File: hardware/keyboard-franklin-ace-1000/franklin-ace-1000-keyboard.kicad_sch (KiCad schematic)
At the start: 161 parts, among them J1 Conn_02x20_Odd_Even, K1 ESC, K10 A, K11 Z, K12 2 @, K13 W, K14 S, K15 X, K16 3 #, K17 E, K18 D, K19 C, K2 BREAK, K20 4 $, K21 R, K22 F, K23 V, K24 5 &, K25 T, K26 G, K27 B, K28 6 ^, K29 Y, K3 PAUSE, K30 H, K31 N, K32 SPACE_8U, K33 7 &, K34 U, K35 J, K36 M, K37 8 *, K38 I, K39 K, K4 CTRL, K40 , <, K41 9 (, K42 O, K43 L, K44 . >, K45 RIGHT, K46 -, K47 +, K48 *, K49 0 ), K5 TAB, K50 P, K51 ; :, K52 / ?, K53 7, K54 4, K55 1, K56 >, K57 - / _, K58 [ {, K59 ; ", K6 LOCK, K60 SHIFT, K61 8, K62 5, K63 2, K64 0, K65 + / =, K66 ] }, K67 RETURN, K68 LEFT, K69 9, K7 SHIFT, K70 6, K71 3, K72 ., K73 SPACE_1U, K74 TAB2, K8 1 !, K9 Q

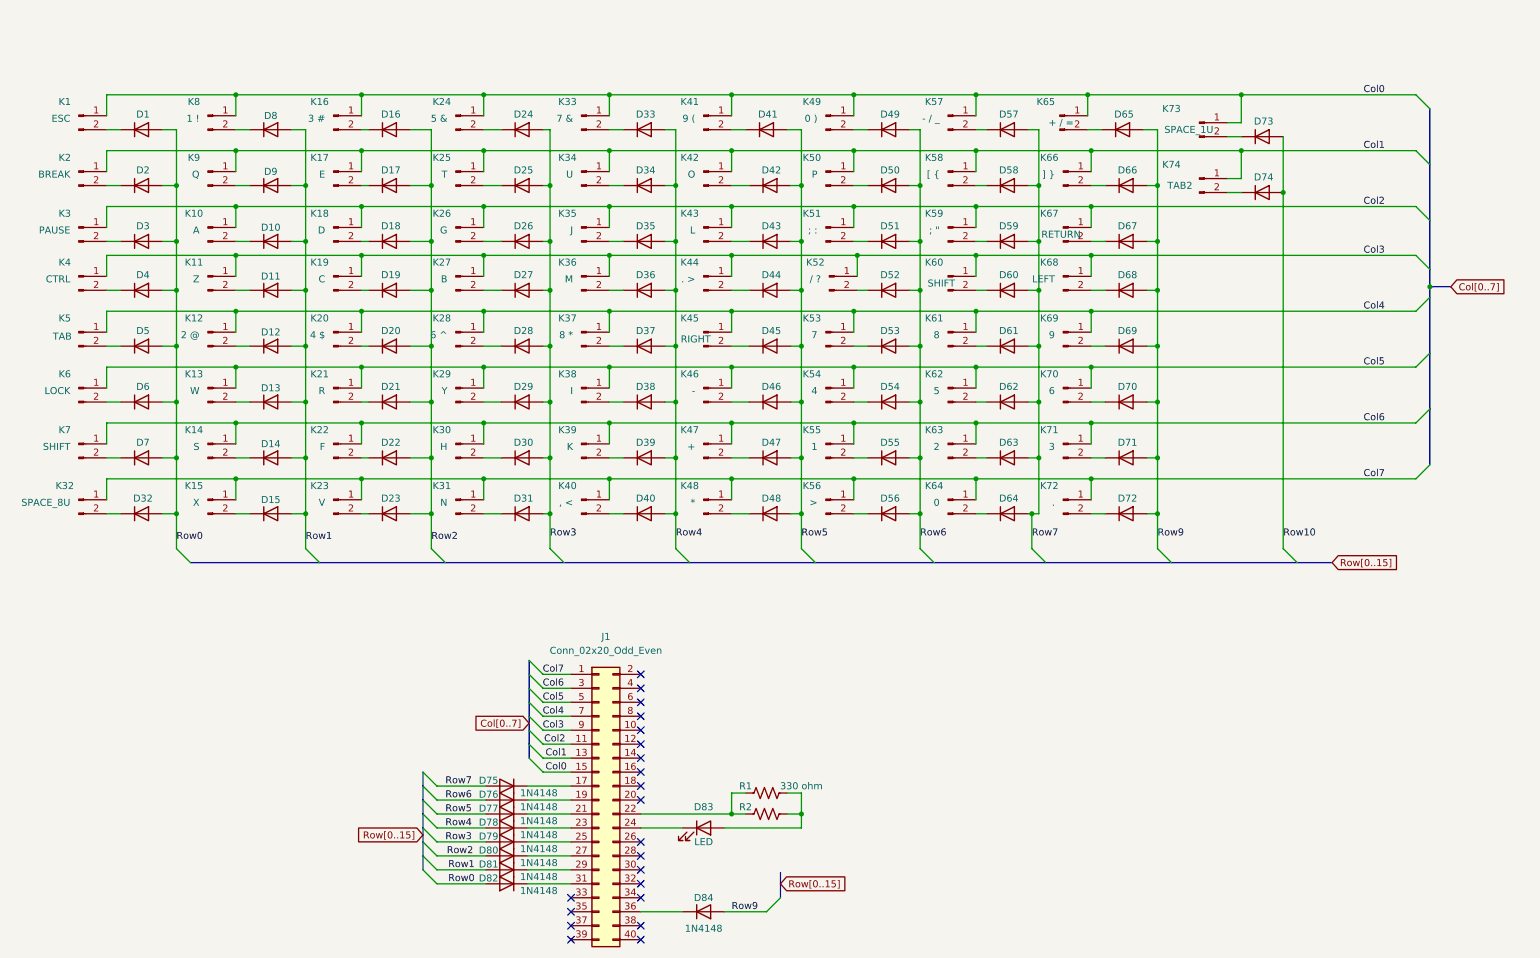
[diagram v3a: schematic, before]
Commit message: True up Franklin 1000 key spacing
- Make sure each 1U is 0.75 inch.
- Record key width for all keys > 1U, and ensure spacing is correct.
- create symbols for the mx keys
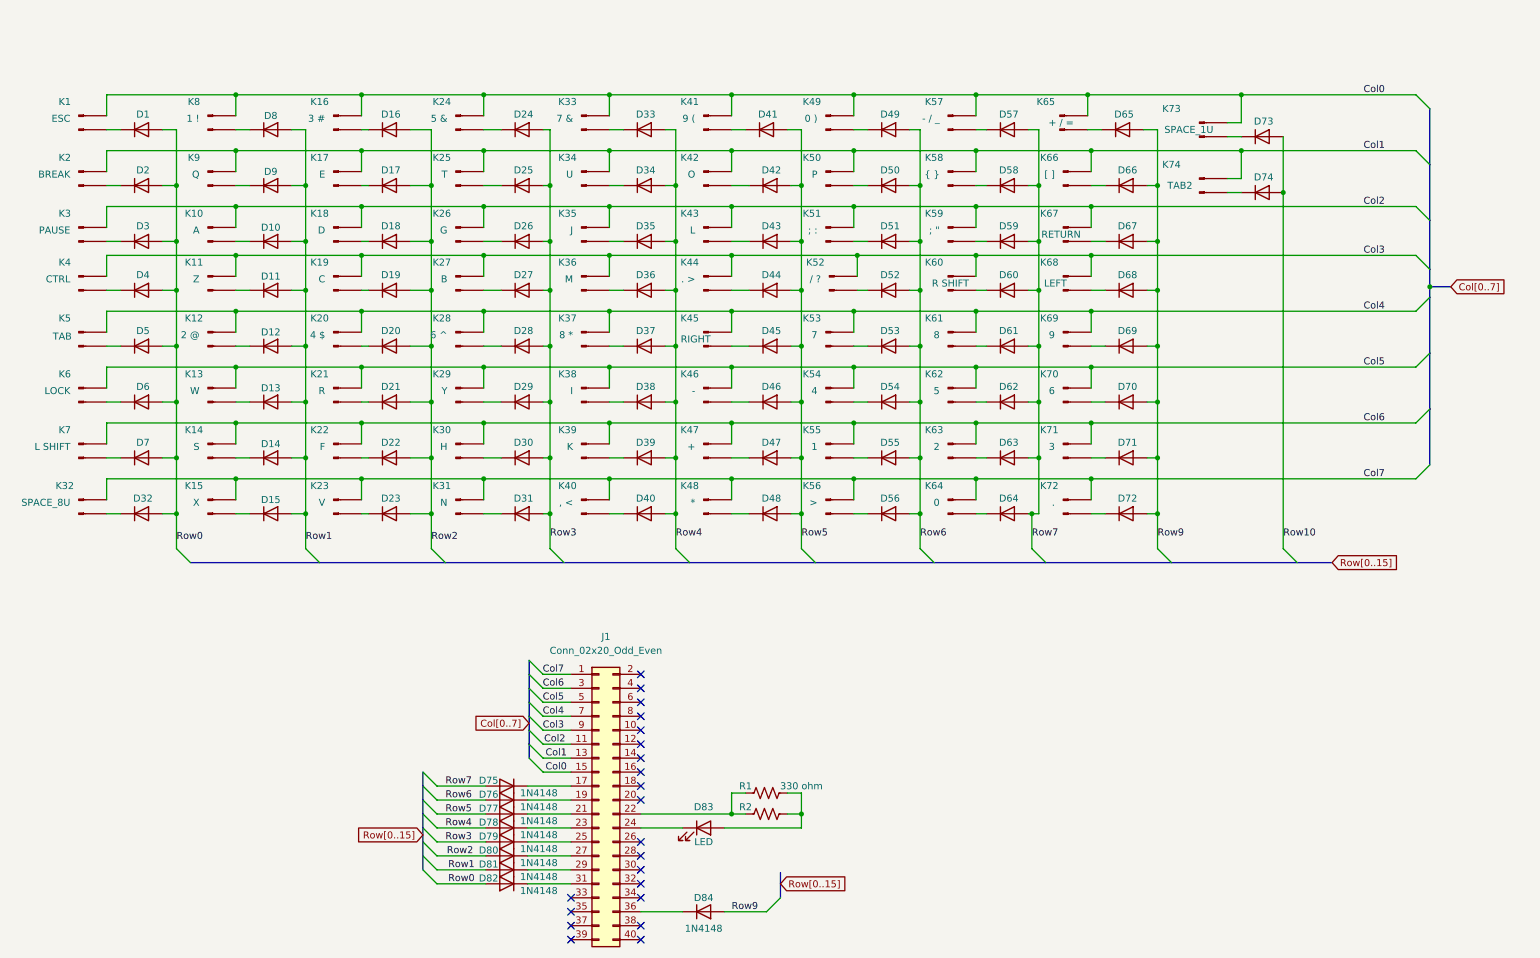
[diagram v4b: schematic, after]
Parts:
- K1, K10, K11, K12, K13, K14, K15, K16, K17, K18, K19, K2, K20, K21, K22, K23, K24, K25, K26, K27, K28, K29, K3, K30, K31, K33, K34, K35, K36, K37, K38, K39, K4, K40, K41, K42, K43, K44, K45, K46, K47, K48, K49, K50, K51, K52, K53, K55, K56, K57, K59, K61, K62, K63, K64, K65, K69, K70, K71, K72, K73, K74, K8, K9: symbol Connector:Conn_01x02_Pin -> unikbd:SW Cherry MX/Futaba 1U Style B; Allow Substitution (none) -> Yes; Class (none) -> If applicable; Component Type (none) -> Switch; Component Value (none) -> Key; Fitted (none) -> Yes; Manufacturer (none) -> Cherry; Manufacturer Link (none) -> https://www.cherrymx.de/en/cherry-mx/mx-original/mx-black.h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; Manufacturer PN (none) -> MX1A-11NN; Material (none) -> If applicable; Number of Pins (none) -> 2; Power Rating (none) -> 10 mA; RoHS (none) -> Yes; RoHS Document Link (none) -> https://www.mouser.com/catalog/additional/Cherry_Electrical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; Standards Version (none) -> 1.1; Temp (Operating) (none) -> -40C/+170C; Temp (Soldering) (none) -> If applicable; Temp Coeff. (none) -> If applicable; Tolerance (none) -> If applicable; Tracking (none) -> No
- K32: symbol Connector:Conn_01x02_Pin -> unikbd:SW Cherry MX/Futaba 8U Spacebar Style B; Allow Substitution (none) -> Yes; Class (none) -> If applicable; Component Type (none) -> Switch; Component Value (none) -> Key; Fitted (none) -> Yes; Manufacturer (none) -> Cherry; Manufacturer Link (none) -> https://www.cherrymx.de/en/cherry-mx/mx-original/mx-black.h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; Manufacturer PN (none) -> MX1A-11NN; Material (none) -> If applicable; Number of Pins (none) -> 2; Power Rating (none) -> 10 mA; RoHS (none) -> Yes; RoHS Document Link (none) -> https://www.mouser.com/catalog/additional/Cherry_Electrical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; Standards Version (none) -> 1.1; Temp (Operating) (none) -> -40C/+170C; Temp (Soldering) (none) -> If applicable; Temp Coeff. (none) -> If applicable; Tolerance (none) -> If applicable; Tracking (none) -> No
- K5, K67: symbol Connector:Conn_01x02_Pin -> unikbd:SW Cherry MX/Futaba 1U Style B; Allow Substitution (none) -> Yes; BOM Comment (none) -> 1.5U; Class (none) -> If applicable; Component Type (none) -> Switch; Component Value (none) -> Key; Fitted (none) -> Yes; Manufacturer (none) -> Cherry; Manufacturer Link (none) -> https://www.cherrymx.de/en/cherry-mx/mx-original/mx-black.h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; Manufacturer PN (none) -> MX1A-11NN; Material (none) -> If applicable; Number of Pins (none) -> 2; Power Rating (none) -> 10 mA; RoHS (none) -> Yes; RoHS Document Link (none) -> https://www.mouser.com/catalog/additional/Cherry_Electrical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; Standards Version (none) -> 1.1; Temp (Operating) (none) -> -40C/+170C; Temp (Soldering) (none) -> If applicable; Temp Coeff. (none) -> If applicable; Tolerance (none) -> If applicable; Tracking (none) -> No
- K54: symbol Connector:Conn_01x02_Pin -> unikbd:SW Cherry MX/Futaba 1U Style B; Allow Substitution (none) -> Yes; BOM Comment (none) -> 2.25 U spacing; Class (none) -> If applicable; Component Type (none) -> Switch; Component Value (none) -> Key; Fitted (none) -> Yes; Manufacturer (none) -> Cherry; Manufacturer Link (none) -> https://www.cherrymx.de/en/cherry-mx/mx-original/mx-black.h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; Manufacturer PN (none) -> MX1A-11NN; Material (none) -> If applicable; Number of Pins (none) -> 2; Power Rating (none) -> 10 mA; RoHS (none) -> Yes; RoHS Document Link (none) -> https://www.mouser.com/catalog/additional/Cherry_Electrical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; Standards Version (none) -> 1.1; Temp (Operating) (none) -> -40C/+170C; Temp (Soldering) (none) -> If applicable; Temp Coeff. (none) -> If applicable; Tolerance (none) -> If applicable; Tracking (none) -> No
- K58: value [ { -> { }; symbol Connector:Conn_01x02_Pin -> unikbd:SW Cherry MX/Futaba 1U Style B; Allow Substitution (none) -> Yes; Class (none) -> If applicable; Component Type (none) -> Switch; Component Value (none) -> Key; Fitted (none) -> Yes; Manufacturer (none) -> Cherry; Manufacturer Link (none) -> https://www.cherrymx.de/en/cherry-mx/mx-original/mx-black.h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; Manufacturer PN (none) -> MX1A-11NN; Material (none) -> If applicable; Number of Pins (none) -> 2; Power Rating (none) -> 10 mA; RoHS (none) -> Yes; RoHS Document Link (none) -> https://www.mouser.com/catalog/additional/Cherry_Electrical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; Standards Version (none) -> 1.1; Temp (Operating) (none) -> -40C/+170C; Temp (Soldering) (none) -> If applicable; Temp Coeff. (none) -> If applicable; Tolerance (none) -> If applicable; Tracking (none) -> No
- K6: symbol Connector:Conn_01x02_Pin -> unikbd:SW Cherry MX/Futaba 1U Style B; Allow Substitution (none) -> Yes; BOM Comment (none) -> 1.75U; Class (none) -> If applicable; Component Type (none) -> Switch; Component Value (none) -> Key; Fitted (none) -> Yes; Manufacturer (none) -> Cherry; Manufacturer Link (none) -> https://www.cherrymx.de/en/cherry-mx/mx-original/mx-black.h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; Manufacturer PN (none) -> MX1A-11NN; Material (none) -> If applicable; Number of Pins (none) -> 2; Power Rating (none) -> 10 mA; RoHS (none) -> Yes; RoHS Document Link (none) -> https://www.mouser.com/catalog/additional/Cherry_Electrical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; Standards Version (none) -> 1.1; Temp (Operating) (none) -> -40C/+170C; Temp (Soldering) (none) -> If applicable; Temp Coeff. (none) -> If applicable; Tolerance (none) -> If applicable; Tracking (none) -> No
- K60: value SHIFT -> R SHIFT; symbol Connector:Conn_01x02_Pin -> unikbd:SW Cherry MX/Futaba 1U Style B; Allow Substitution (none) -> Yes; BOM Comment (none) -> 2U; Class (none) -> If applicable; Component Type (none) -> Switch; Component Value (none) -> Key; Fitted (none) -> Yes; Manufacturer (none) -> Cherry; Manufacturer Link (none) -> https://www.cherrymx.de/en/cherry-mx/mx-original/mx-black.h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; Manufacturer PN (none) -> MX1A-11NN; Material (none) -> If applicable; Number of Pins (none) -> 2; Power Rating (none) -> 10 mA; RoHS (none) -> Yes; RoHS Document Link (none) -> https://www.mouser.com/catalog/additional/Cherry_Electrical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; Standards Version (none) -> 1.1; Temp (Operating) (none) -> -40C/+170C; Temp (Soldering) (none) -> If applicable; Temp Coeff. (none) -> If applicable; Tolerance (none) -> If applicable; Tracking (none) -> No
- K66: value ] } -> [ ]; symbol Connector:Conn_01x02_Pin -> unikbd:SW Cherry MX/Futaba 1U Style B; Allow Substitution (none) -> Yes; BOM Comment (none) -> 1.75U; Class (none) -> If applicable; Component Type (none) -> Switch; Component Value (none) -> Key; Fitted (none) -> Yes; Manufacturer (none) -> Cherry; Manufacturer Link (none) -> https://www.cherrymx.de/en/cherry-mx/mx-original/mx-black.h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; Manufacturer PN (none) -> MX1A-11NN; Material (none) -> If applicable; Number of Pins (none) -> 2; Power Rating (none) -> 10 mA; RoHS (none) -> Yes; RoHS Document Link (none) -> https://www.mouser.com/catalog/additional/Cherry_Electrical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; Standards Version (none) -> 1.1; Temp (Operating) (none) -> -40C/+170C; Temp (Soldering) (none) -> If applicable; Temp Coeff. (none) -> If applicable; Tolerance (none) -> If applicable; Tracking (none) -> No
- K68: symbol Connector:Conn_01x02_Pin -> unikbd:SW Cherry MX/Futaba 1U Style B; Allow Substitution (none) -> Yes; BOM Comment (none) -> 1.25U; BOM comment (none) -> 2.25U; Class (none) -> If applicable; Component Type (none) -> Switch; Component Value (none) -> Key; Fitted (none) -> Yes; Manufacturer (none) -> Cherry; Manufacturer Link (none) -> https://www.cherrymx.de/en/cherry-mx/mx-original/mx-black.h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; Manufacturer PN (none) -> MX1A-11NN; Material (none) -> If applicable; Number of Pins (none) -> 2; Power Rating (none) -> 10 mA; RoHS (none) -> Yes; RoHS Document Link (none) -> https://www.mouser.com/catalog/additional/Cherry_Electrical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; Standards Version (none) -> 1.1; Temp (Operating) (none) -> -40C/+170C; Temp (Soldering) (none) -> If applicable; Temp Coeff. (none) -> If applicable; Tolerance (none) -> If applicable; Tracking (none) -> No
- K7: value SHIFT -> L SHIFT; symbol Connector:Conn_01x02_Pin -> unikbd:SW Cherry MX/Futaba 2U Style B; Allow Substitution (none) -> Yes; BOM Comment (none) -> 2.25U; Class (none) -> If applicable; Component Type (none) -> Switch; Component Value (none) -> Key; Fitted (none) -> Yes; Manufacturer (none) -> Cherry; Manufacturer Link (none) -> https://www.cherrymx.de/en/cherry-mx/mx-original/mx-black.h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; Manufacturer PN (none) -> MX1A-11NN; Material (none) -> If applicable; Number of Pins (none) -> 2; Power Rating (none) -> 10 mA; RoHS (none) -> Yes; RoHS Document Link (none) -> https://www.mouser.com/catalog/additional/Cherry_Electrical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; Standards Version (none) -> 1.1; Temp (Operating) (none) -> -40C/+170C; Temp (Soldering) (none) -> If applicable; Temp Coeff. (none) -> If applicable; Tolerance (none) -> If applicable; Tracking (none) -> No
